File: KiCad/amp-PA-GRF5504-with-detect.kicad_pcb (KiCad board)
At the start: 4 copper layers, 44 x 34 mm, 51 parts, among them J1 142-0701-851, J2 142-0701-851, Q1 P-CH, Q2 N-CH, U2 BDCN-20-13+, U3 LT5534, U4 LT5534, U5 GRF5504

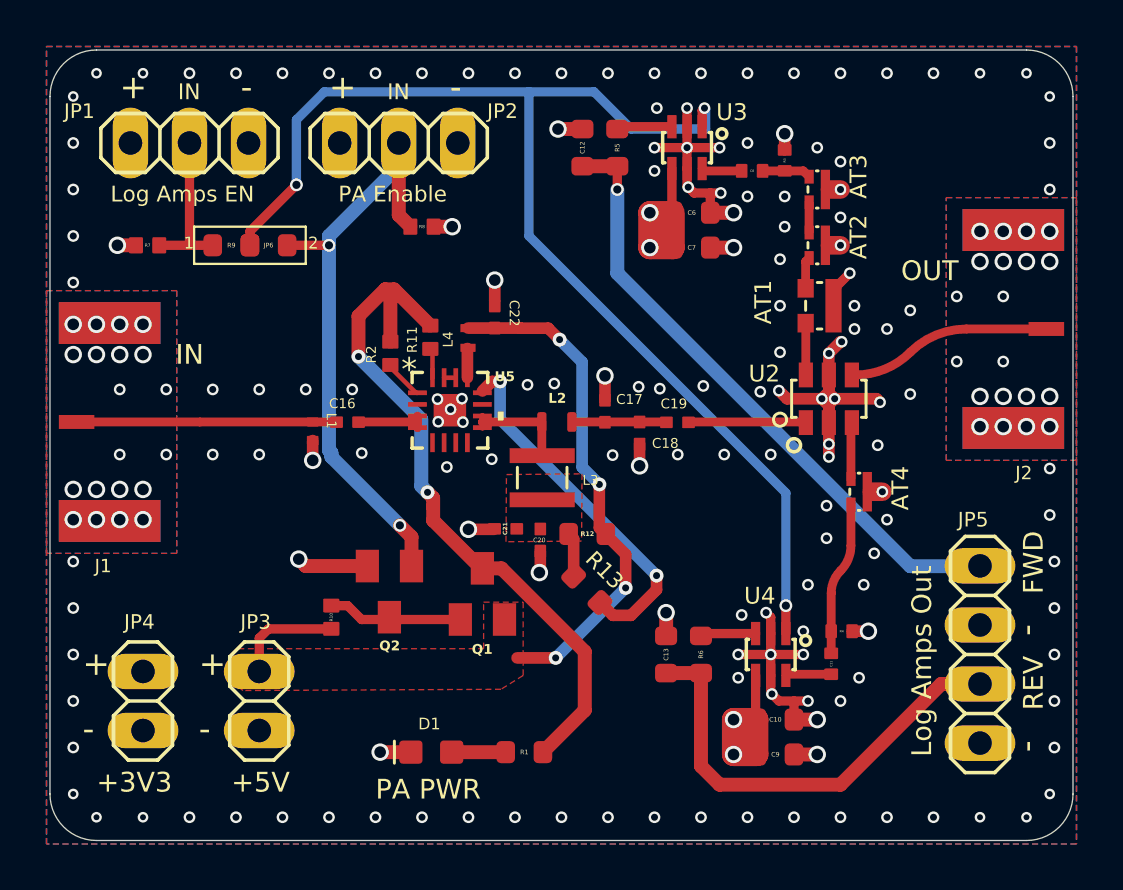
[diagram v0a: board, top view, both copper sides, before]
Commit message: cleared some of the DRC errors
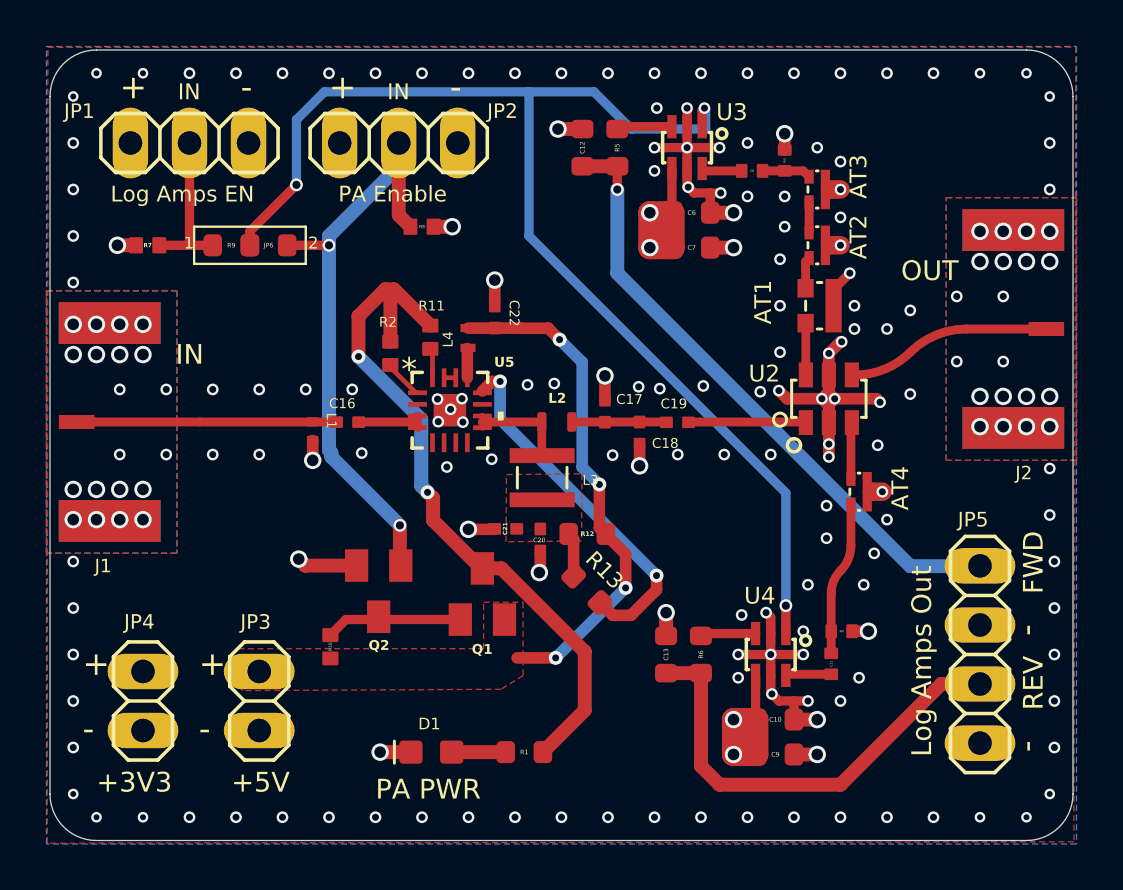
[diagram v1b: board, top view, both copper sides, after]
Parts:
- J1, J2: value 142-0701-851 -> (none)
- moved R10 1.27 mm to (138.6, 113.7)
- moved Q2 0.46 mm to (140.6, 111.3)
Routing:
- net +5V: track 27.1 -> 22.4 mm
- removed copper zone on In2.Cu, net GND
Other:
- board text added: "UHF 3.5W Power Amplifier 436.5 MHz - GRF5504 PSAS / OreSat 2026-22-02 v1.0 J.D.L.S.R."
- board text removed: "UHF 3.5W Power Amplifier 436.5 MHz - GRF5504 PSAS / OreSat 2020-08-01 v1.0 E.M. KJ7AOG"

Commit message: cleared all ERC warnings
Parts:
- U2: value BDCN-20-13+ -> (none)
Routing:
- net GND: track 51.8 -> 56.8 mm, vias 199 -> 200

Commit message: cleared some of the DRC errors
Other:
- rule pad_to_mask_clearance: 0 -> 0.0508
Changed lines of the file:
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@@
 			(dielectric_constraints no)
 		)
-		(pad_to_mask_clearance 0)
+		(pad_to_mask_clearance 0.0508)
 		(allow_soldermask_bridges_in_footprints no)
 		(tenting front back)
@@
 			(layer "F.Fab")
 		)
-		(fp_text user "${REFERENCE}"
-			(at 0 0 270)
-			(unlocked yes)
-			(layer "F.Mask")
-			(effects
-				(font
-					(size 0.17 0.17)
-					(thickness 0.03)
-				)
-			)
-		)
 		(pad "1" smd roundrect
 			(at -0.475 0 270)
@@
 	)
 	(gr_text "UHF 3.5W Power Amplifier\n436.5 MHz - GRF5504\nPSAS / OreSat\n2026-22-02  v1.0\nJ.D.L.S.R."
-		(at 162.58 119.86 0)
+		(at 163.91 119.48 0)
 		(layer "B.SilkS")
 		(effects

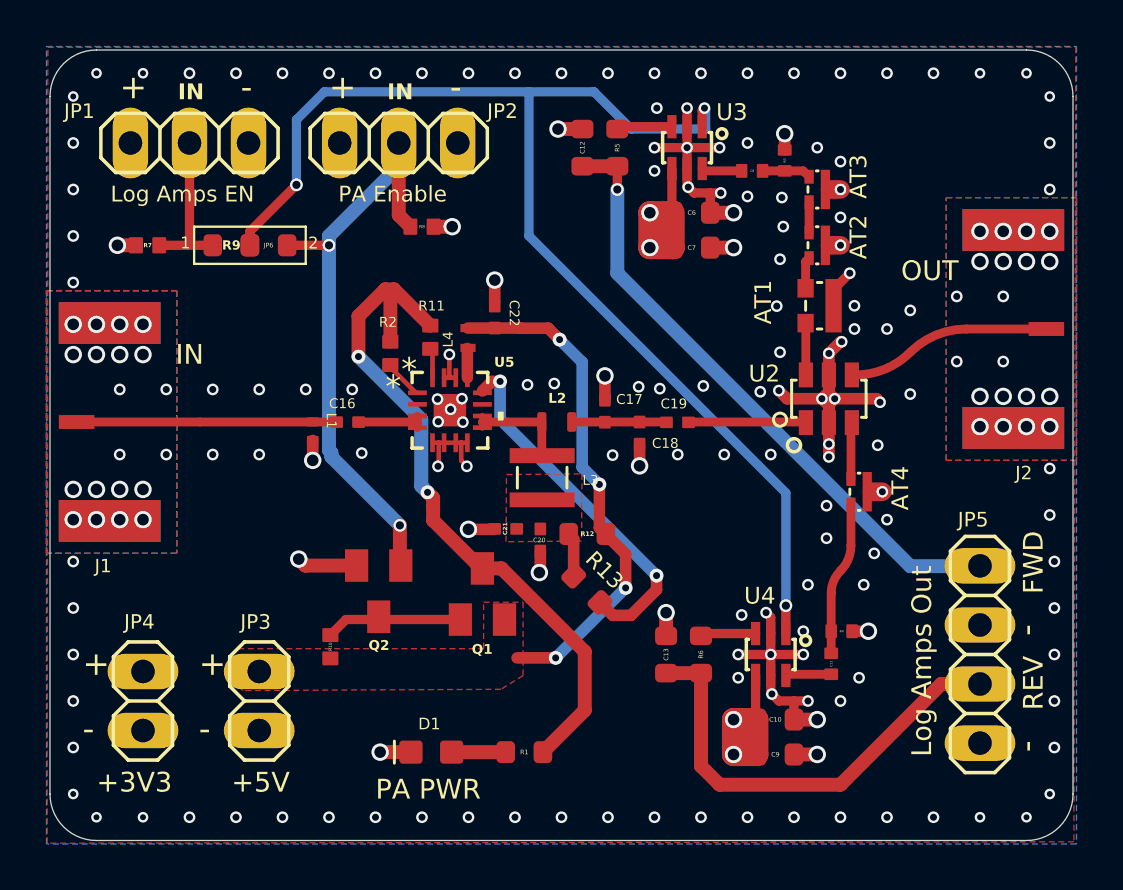
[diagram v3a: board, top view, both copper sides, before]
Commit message: Excluded remaining DRC errors
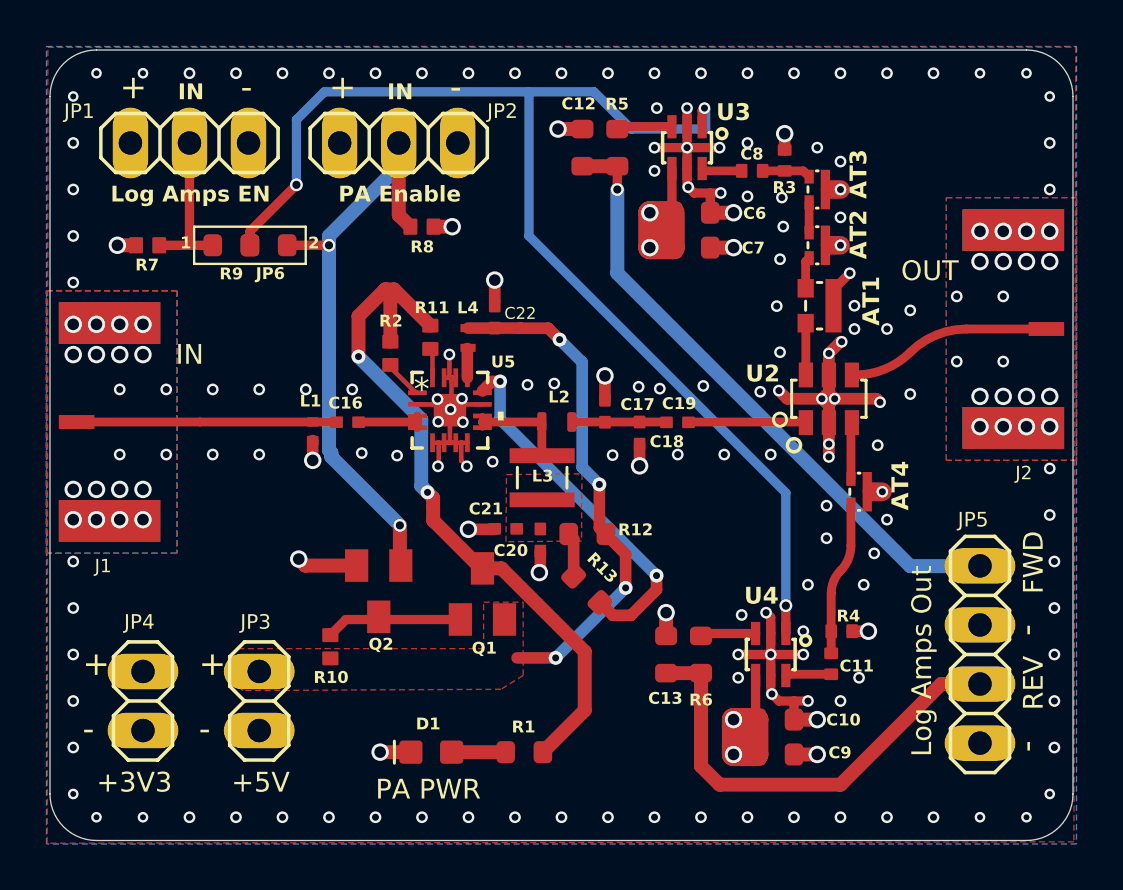
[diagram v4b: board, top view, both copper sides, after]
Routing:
- net GND: track 56.8 -> 62.5 mm, vias 200 -> 202
